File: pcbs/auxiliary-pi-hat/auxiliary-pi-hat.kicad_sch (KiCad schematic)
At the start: 18 parts, among them J1 Conn_01x02, J2 Raspberry Pi - Hat Template -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, J3 Conn_01x03, J4 Conn_01x03, J5 Conn_01x03, J6 Conn_01x03, J7 Conn_01x03, J8 Conn_01x04, J9 Conn_01x05, SW1 SW_Push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

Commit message: aux pcb update
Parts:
- removed DISP1: ~, displays:TFT LCD - 2.4 - 240x320, symbol displays:TFT_LCD_-_2.4_-_240x320
- removed J6, J7: Conn_01x03, Connector_JST:JST_ZH_B3B-ZR_1x03_P1.50mm_Vertical, symbol Connector_Generic:Conn_01x03
- removed J8: Conn_01x04, Connector_PinHeader_2.54mm:PinHeader_1x04_P2.54mm_Horizontal, symbol Connector_Generic:Conn_01x04
- removed R2, R4: R_Small_US, Resistor_SMD:R_1206_3216Metric, symbol Device:R_Small_US
- removed SW2: SW_Push, Button_Switch_THT:SW_PUSH_6mm_H4.3mm, symbol Switch:SW_Push
- added DISP1: ~, displays:LCD-Display-1.8-128x160-Hiletgo, symbol displays:LCD-Display-1.8-128x160-Hiletgo
- added J10, J11: Conn_01x03, Connector_JST:JST_ZH_B3B-ZR_1x03_P1.50mm_Vertical, symbol Connector_Generic:Conn_01x03
- added J7: Conn_01x04, Connector_JST:JST_ZH_B4B-ZR_1x04_P1.50mm_Vertical, symbol Connector_Generic:Conn_01x04
- added J8: Conn_02x04_Odd_Even, Connector_PinHeader_2.54mm:PinHeader_2x04_P2.54mm_Vertical, symbol Connector_Generic:Conn_02x04_Odd_Even
- added Q1, Q2: BSS138, Package_TO_SOT_SMD:SOT-23, symbol Transistor_FET:BSS138
- added R5, R6, R7, R8: 10k, Resistor_SMD:R_1206_3216Metric, symbol Device:R_Small_US
- added R9: 500, Resistor_SMD:R_1206_3216Metric, symbol Device:R_Small_US
- added U2: SN74LVC1G14DBV, Package_TO_SOT_SMD:SOT-23-5, symbol 74xGxx:SN74LVC1G14DBV
- J9: footprint Connector_PinHeader_2.54mm:PinHeader_1x05_P2.54mm_Horizontal -> Connector_JST:JST_ZH_B5B-ZR_1x05_P1.50mm_Vertical
- R3: value R_Small_US -> 500
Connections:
- net +3.3V: now also J4.1 (Pin_1), DISP1.1 (VCC), DISP1.8 (LED), J7.1 (Pin_1), Q1.1 (G), Q2.1 (G), R6.2, R7.2
- net +5V: now also J10.1 (Pin_1), J11.1 (Pin_1), R5.2, R8.2, U2.5 (VCC); no longer J4.1 (Pin_1)
- net GND: now also DISP1.2 (GND), J10.3 (Pin_3), J11.3 (Pin_3), J7.4 (Pin_4), J8.2 (Pin_2), J8.4 (Pin_4), J8.6 (Pin_6), J8.8 (Pin_8), U2.3 (GND)
- net GPIO-2: now also J4.2 (Pin_2); no longer U1.3 (PB14)
- net NEO-0: now also Q2.2 (S), R7.1; no longer R3.1
- net NEO-1: now also Q1.2 (S), R6.1
- net SCL: now also J2.05 (GPIO03/SCL); no longer U1.14 (PB6)
- net SDA: now also J2.03 (GPIO02/SDA1); no longer U1.15 (PB7)
- net TFT-CS: now also DISP1.3 (CS)
- net TFT-DC: now also DISP1.5 (DC/A0)
- net TFT-MOSI: now also DISP1.6 (MOSI)
- net TFT-RESET: now also DISP1.4 (RST)
- net TFT-SCK: now also DISP1.7 (SCK)
- net SBUS: now reaches J2.29 (GPIO05)
- net SBUS: now also U2.2
- net GPIO-13: now reaches J2.33 (GPIO13)
- net GPIO-13: now also J8.5 (Pin_5)
- net GPIO-16: now reaches J2.36 (GPIO16)
- net GPIO-16: now also J8.3 (Pin_3)
- net GPIO-26: now reaches J2.37 (GPIO26)
- net GPIO-26: now also J8.7 (Pin_7)
- net GPIO-20: now reaches J2.38 (GPIO20)
- net GPIO-20: now also J8.1 (Pin_1)
- net ADC-0: no longer names the net of U1.26 (PA0)
- net BTN-2: no longer names the net of U1.17 (PB9)
- net GPIO-0 renamed GPIO-17
- net GPIO-1: no longer names the net of J2.13 (GPIO27)
- net GPIO-1: no longer U1.2 (PB13)
- net TFT-MISO: no longer names the net of U1.32 (PA6)
- new net: J11.2 (Pin_2), U2.4
- new net: Q2.3 (D), R8.1, R9.1
- new net: J10.2 (Pin_2), R9.2
- new net: Q1.3 (D), R3.1, R5.1
- new net SCL_MCU: J7.3 (Pin_3), U1.14 (PB6)
- new net SDA_MCU: J7.2 (Pin_2), U1.15 (PB7)
- no-connect marks 49 -> 36
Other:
- note added: "FOOT CONTACTS"
- note added: "FrSky Receiver"
- note removed: "ADC"
- moved on the sheet: J2, J3, J5, J9, R1, R3, SW1

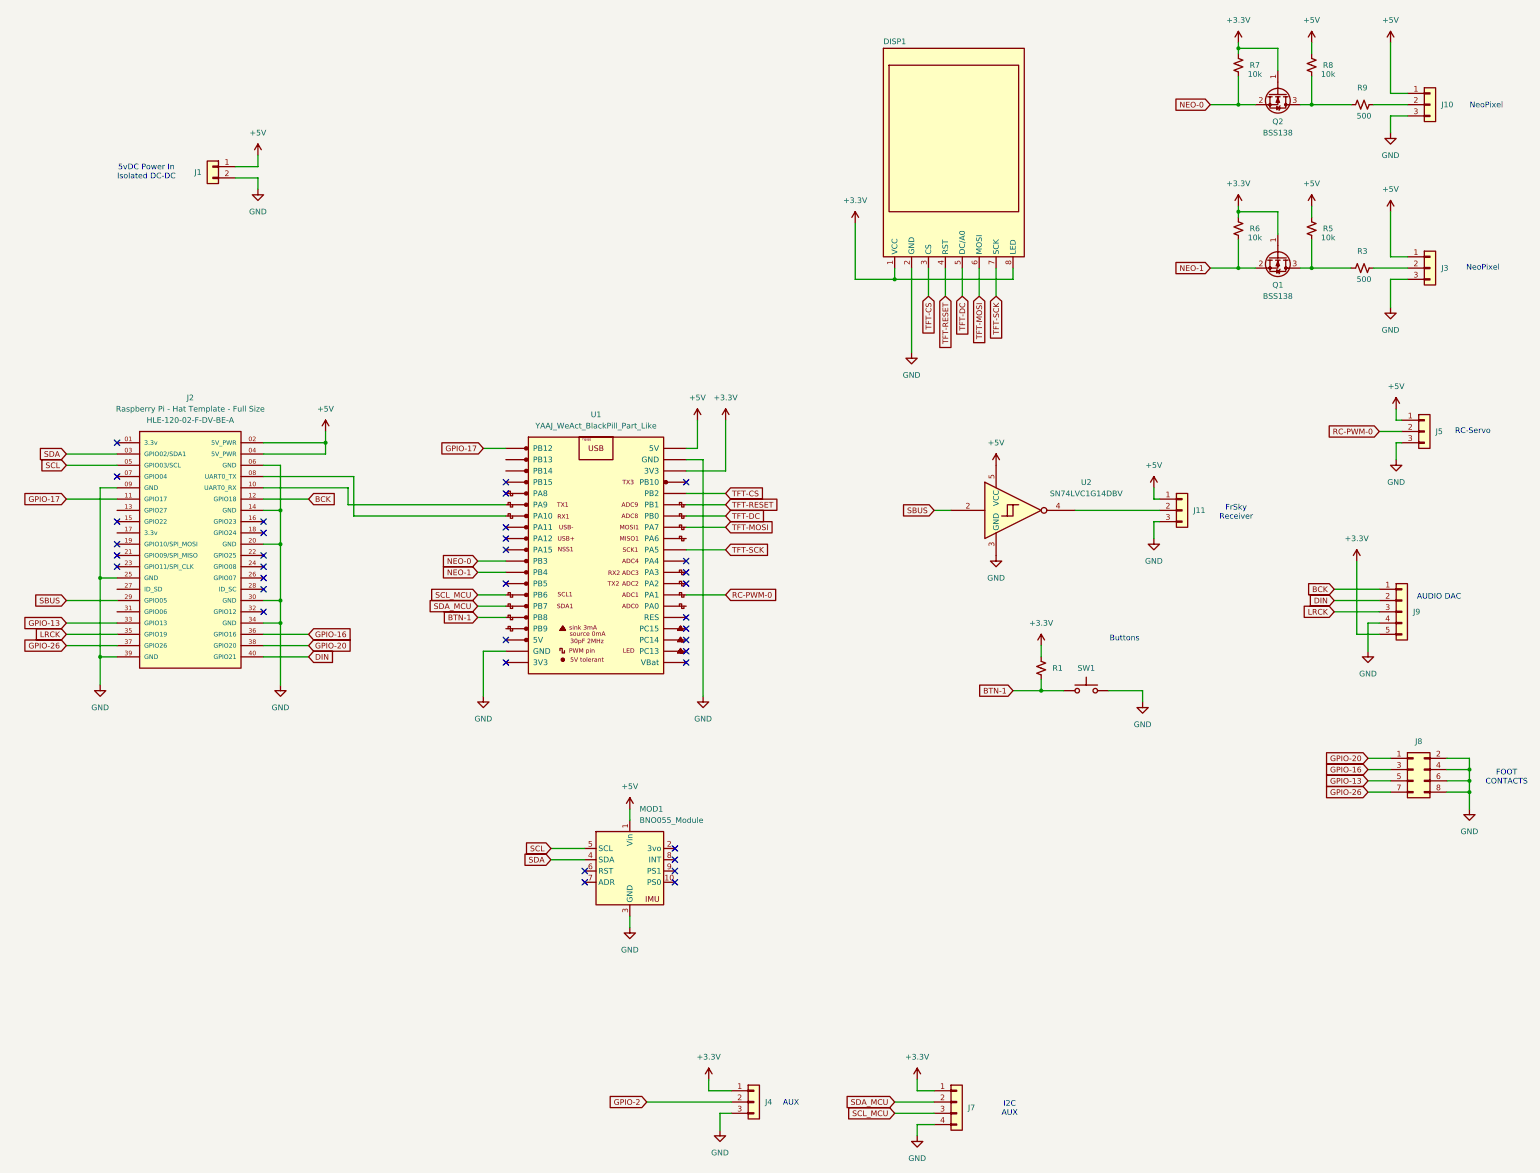
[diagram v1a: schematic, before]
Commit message: motor source upload; file reorg
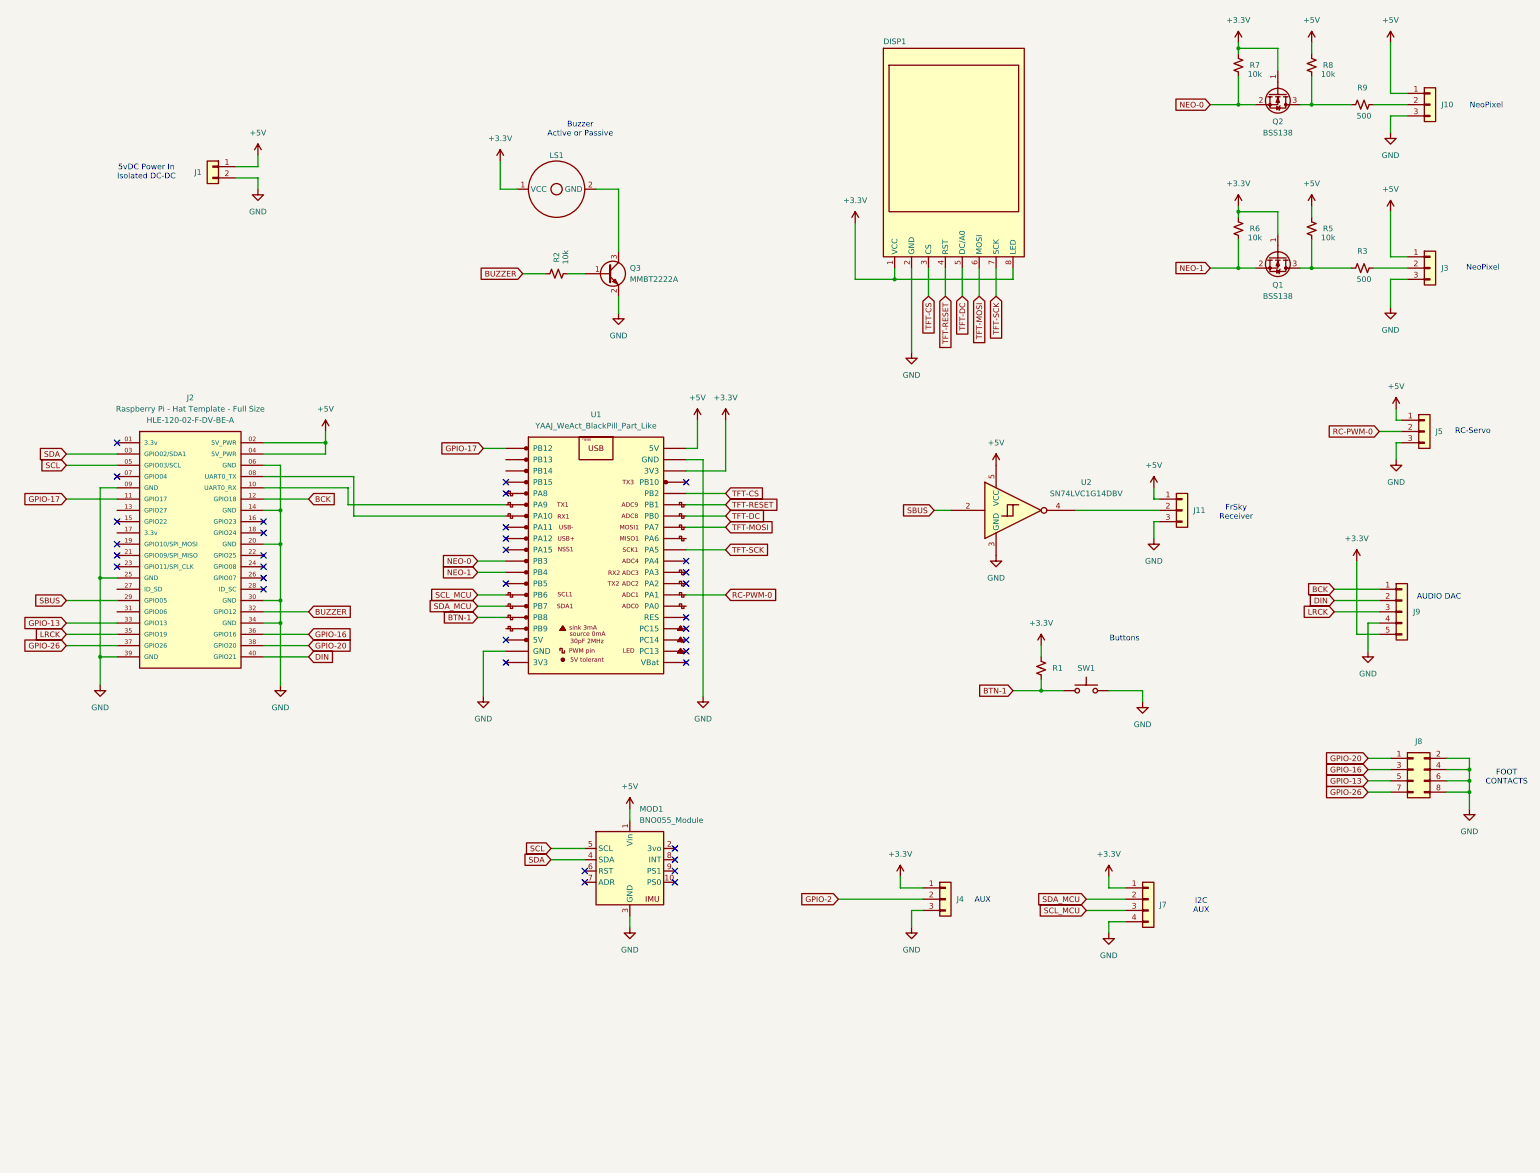
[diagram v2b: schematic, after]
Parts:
- added LS1: ~, general:PB-09N23P-03Q_MAL, symbol General:PB_09N23P_03Q
- added Q3: MMBT2222A, Package_TO_SOT_SMD:SOT-23, symbol Transistor_BJT:MMBT2222A
- added R2: 10k, Resistor_SMD:R_1206_3216Metric, symbol Device:R_Small_US
- J1: footprint TerminalBlock_Phoenix:TerminalBlock_Phoenix_PT-1,5-2-5.0-H_1x02_P5.00mm_Horizontal -> TerminalBlock_Phoenix:TerminalBlock_Phoenix_PT-1,5-2-3.5-H_1x02_P3.50mm_Horizontal
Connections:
- net +3.3V: now also LS1.1 (VCC)
- net GND: now also Q3.2 (E)
- net BUZZER: now reaches J2.32 (GPIO12)
- net BUZZER: now also R2.2
- new net: LS1.2 (GND), Q3.3 (C)
- new net: Q3.1 (B), R2.1
- no-connect marks 36 -> 35
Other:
- note added: "Buzzer Active or Passive"
- moved on the sheet: J4, J7

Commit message: PCB update
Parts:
- added JP1: Jumper_3_Open, Jumper:SolderJumper-3_P1.3mm_Open_Pad1.0x1.5mm, symbol Jumper:Jumper_3_Open
- added R10, R11, R12, R4: 10k, Resistor_SMD:R_1206_3216Metric, symbol Device:R_Small_US
- J2: footprint General:Raspberry Pi - Hat Template - Full Size -> sbcs:Raspberry Pi - Hat Template - Full Size Extended
- MOD1: footprint General:BNO055 Module -> general:BNO055 Module
- U1: footprint MCU_Modules:YAAJ_WeAct_BlackPill_2 -> mcus:Blackpill WeAct
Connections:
- net +3.3V: now also U2.5 (VCC)
- net +5V: no longer U2.5 (VCC)
- net BTN-1: now also U1.23 (PC14); no longer U1.16 (PB8)
- net GPIO-13: now also R11.1
- net GPIO-16: now also R10.1
- net GPIO-20: now also R4.1
- net GPIO-26: now also R12.1
- net RC-PWM-0: now also U1.5 (PA8); no longer U1.27 (PA1)
- net 3v3-RPI: now reaches J2.17 (3.3v)
- net 3v3-RPI: now also R10.2, R11.2, R12.2, R4.2
- net BUZZER_MCU: now reaches U1.17 (PB9)
- net BUZZER_MCU: now also JP1.3 (B)
- net BUZZER: no longer names the net of R2.2
- net BUZZER: now also JP1.2 (C); no longer J2.32 (GPIO12)
- net GPIO-2 renamed AUX
- net AUX: now also U1.16 (PB8)
- new net BUZZER_RPI: J2.32 (GPIO12), JP1.1 (A)
- no-connect marks 35 -> 41
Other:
- moved on the sheet: J8

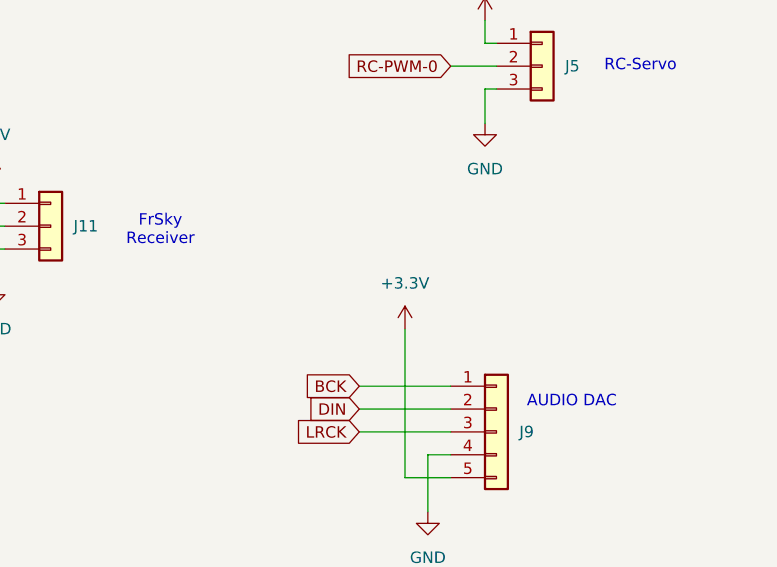
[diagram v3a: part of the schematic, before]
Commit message: plot.py update to handle no gamepad connected
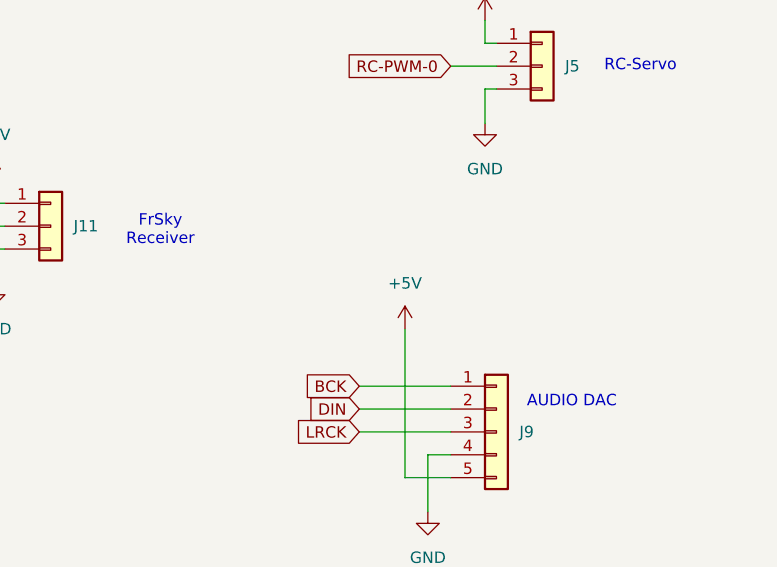
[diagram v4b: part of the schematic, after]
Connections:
- net +3.3V: no longer J9.5 (Pin_5)
- net +5V: now also J9.5 (Pin_5)
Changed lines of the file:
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@@
 	)
 	(symbol
-		(lib_id "power:+3.3V")
+		(lib_id "power:+5V")
 		(at 330.2 146.05 0)
 		(unit 1)
@@
 			)
 		)
-		(property "Value" "+3.3V"
+		(property "Value" "+5V"
 			(at 330.2 140.97 0)
 			(effects
@@
 			)
 		)
-		(property "Description" "Power symbol creates a global label with name \"+3.3V\""
+		(property "Description" "Power symbol creates a global label with name \"+5V\""
 			(at 330.2 146.05 0)
 			(effects
@@
 		)
 		(instances
-			(project "aux-board"
+			(project "auxiliary-pi-hat"
 				(path "/312efdca-dfe3-4c27-a2ae-6c196f0be09d"
 					(reference "#PWR021")
